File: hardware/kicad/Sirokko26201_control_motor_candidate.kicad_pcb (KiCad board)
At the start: 2 copper layers, 335 x 170 mm, 158 parts, among them J1 DEVKITC1_J1, J10 TC_K_EXHAUST_T+_T-, J102 MOTOR_24V_HIGH_SPEED; 125W_HE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, J11 TC_K_AIR_T+_T-, J12 ROOM_DS18B20_HARNESS, J13 24V_INPUT_PHOENIX_1756993_WIP, J22 START_STOP B3F-4055 + B32-138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, J23 ENCODER EC11E15244G1 + KNOB 4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, J24 RESET NKK BB25AB-FA, J26 TFT CABLE HARWIN M20-9960845 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, J27 GLOW_OUTPUT_PHOENIX_1756993, J28 CLUTCH_OUTPUT_PHOENIX_1756993, J3 DEVKITC1_J3, K1 DG85BM-5021-76-1024 + DZ85AB-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, K2 DG85BM-5021-76-1024 + DZ85AB-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, K3 DG85BM-5021-76-1024 + DZ85AB-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, Q1 IPB017N10N5LFATMA1 WIP, Q101 IRFB4110PBF (100V; RDS(on) @ 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, Q2 IPB017N10N5LFATMA1 WIP, Q20 BC847B,215, Q3 IPB017N10N5LFATMA1 WIP, Q4 IPB017N10N5LFATMA1 WIP, U1 TPS3431SDRBR, U10 MAX31856MUD+, U101 LM5013DDAR, U11 DRV8803PWPR, U13 LM74800QDRRRQ1 WIP_NOT_TRANSI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, U2 SN74HCS74D, U20 SN74LVC1G97DBVR, U301 TPS62162DSGR, U302 TPS3808G33DBVR, U303 74LVC125APW,118 Nexperia ONLY, U6 SN74HCS11D, U9 MAX31856MUD+, U9001 LTC7001IMSE#PBF; MSOP-10 EP, U9002 INA240A1ID, U9003 TLV9020DBVR, U9004 SN74LVC1G32DBVR, U9005 SN74LVC1G08DBVR, U9006 SN74LVC1G08DBVR, U9007 LM317HVT/NOPB TO-220; TJ 0…12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

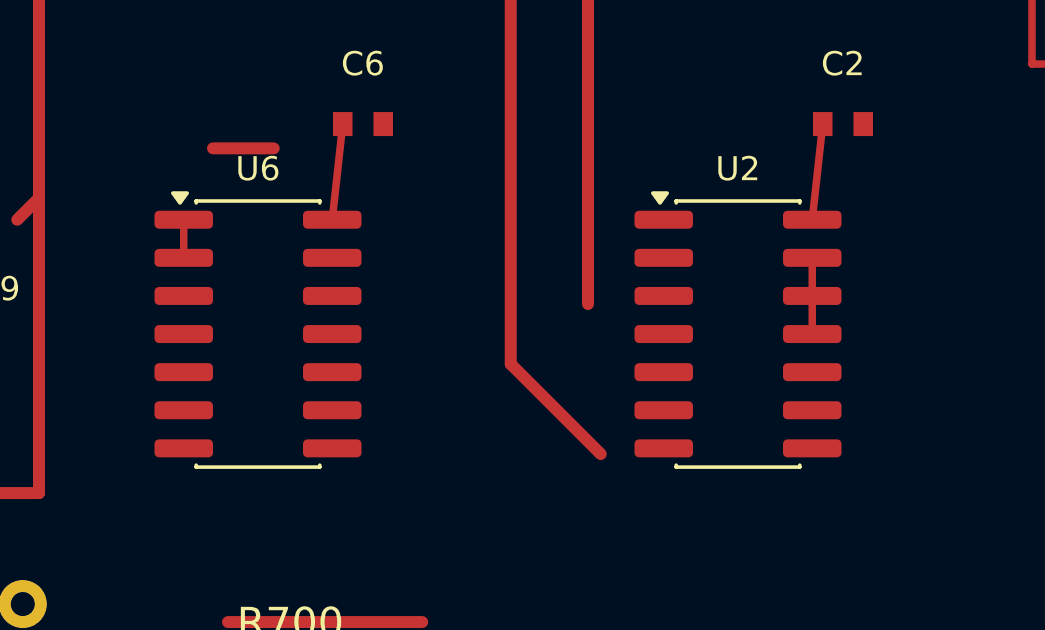
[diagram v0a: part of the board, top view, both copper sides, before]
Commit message: pcb: add after20 logic routing
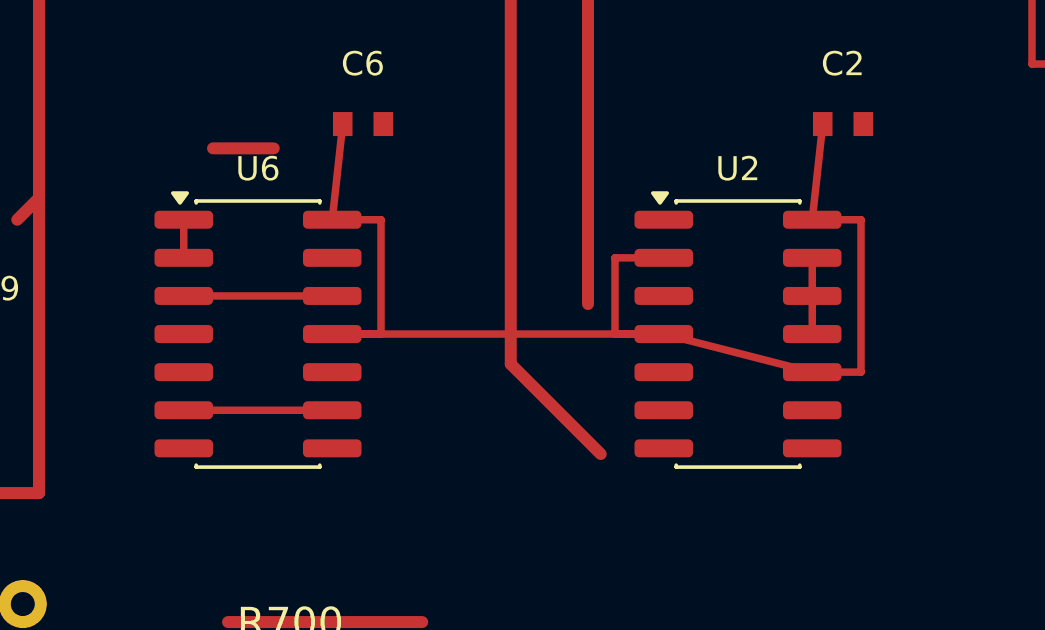
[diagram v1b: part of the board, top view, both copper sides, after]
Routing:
- net /+3V3: track 1245.0 -> 1282.4 mm
- net /MinimalSafety/RESET_POWER_READY: track 0.00 -> 4.95 mm
- net /MinimalSafety/HARD_CONDITIONS_OK: track 0.00 -> 4.95 mm
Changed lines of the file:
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@@
+		(net "/+3V3")
+	)
+	(segment
+		(start 49.475 61.19)
+		(end 51.1 61.19)
+		(width 0.25)
+		(layer "F.Cu")
+		(net "/+3V3")
+	)
+	(segment
+		(start 51.1 61.19)
+		(end 51.1 65)
+		(width 0.25)
+		(layer "F.Cu")
+		(net "/+3V3")
+	)
+	(segment
+		(start 51.1 65)
+		(end 49.475 65)
+		(width 0.25)
+		(layer "F.Cu")
+		(net "/+3V3")
+	)
+	(segment
+		(start 65.475 61.19)
+		(end 67.1 61.19)
+		(width 0.25)
+		(layer "F.Cu")
+		(net "/+3V3")
+	)
+	(segment
+		(start 67.1 61.19)
+		(end 67.1 66.27)
+		(width 0.25)
+		(layer "F.Cu")
+		(net "/+3V3")
+	)
+	(segment
+		(start 67.1 66.27)
+		(end 65.475 66.27)
+		(width 0.25)
+		(layer "F.Cu")
+		(net "/+3V3")
+	)
+	(segment
+		(start 60.525 62.46)
+		(end 58.9 62.46)
+		(width 0.25)
+		(layer "F.Cu")
+		(net "/+3V3")
+	)
+	(segment
+		(start 58.9 62.46)
+		(end 58.9 65)
+		(width 0.25)
+		(layer "F.Cu")
+		(net "/+3V3")
+	)
+	(segment
+		(start 58.9 65)
+		(end 60.525 65)
+		(width 0.25)
+		(layer "F.Cu")
+		(net "/+3V3")
+	)
+	(segment
+		(start 44.525 63.73)
+		(end 49.475 63.73)
+		(width 0.25)
+		(layer "F.Cu")
+		(net "/MinimalSafety/HARD_CONDITIONS_OK")
+	)
+	(segment
+		(start 44.525 67.54)
+		(end 49.475 67.54)
+		(width 0.25)
+		(layer "F.Cu")
+		(net "/MinimalSafety/RESET_POWER_READY")
+	)
+	(segment
+		(start 60.525 65)
+		(end 65.475 66.27)
+		(width 0.25)
+		(layer "F.Cu")
+		(net "/+3V3")
+	)
+	(segment
+		(start 49.475 65)
+		(end 55.425 65)
+		(width 0.25)
+		(layer "F.Cu")
+		(net "/+3V3")
+	)
+	(segment
+		(start 55.425 65)
+		(end 60.525 65)
+		(width 0.25)
+		(layer "F.Cu")
 		(net "/+3V3")
 	)

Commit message: pcb: add after30 routing
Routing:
- net /GND: track 2067.0 -> 2095.8 mm
- net /+3V3: track 1282.4 -> 1289.1 mm
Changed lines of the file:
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@@
 		(net "/+3V3")
+	)
+	(segment
+		(start 44.525 68.81)
+		(end 39.7 70.3)
+		(width 0.25)
+		(layer "F.Cu")
+		(net "/GND")
+	)
+	(segment
+		(start 60.525 68.81)
+		(end 53.16 77)
+		(width 0.25)
+		(layer "F.Cu")
+		(net "/GND")
+	)
+	(segment
+		(start 29.6 64.025)
+		(end 28.7 64.025)
+		(width 0.25)
+		(layer "F.Cu")
+		(net "/+3V3")
+	)
+	(segment
+		(start 28.7 64.025)
+		(end 28.7 65.325)
+		(width 0.25)
+		(layer "F.Cu")
+		(net "/+3V3")
+	)
+	(segment
+		(start 28.7 65.325)
+		(end 29.6 65.325)
+		(width 0.25)
+		(layer "F.Cu")
+		(net "/+3V3")
+	)
+	(segment
+		(start 29.6 64.025)
+		(end 27.675 61)
+		(width 0.25)
+		(layer "F.Cu")
+		(net "/+3V3")
+	)
+	(segment
+		(start 26.325 68.81)
+		(end 28.2 68.81)
+		(width 0.25)
+		(layer "F.Cu")
+		(net "/GND")
+	)
+	(segment
+		(start 26.325 61)
+		(end 24.8 61)
+		(width 0.25)
+		(layer "F.Cu")
+		(net "/GND")
+	)
+	(segment
+		(start 24.8 61)
+		(end 24.8 68.81)
+		(width 0.25)
+		(layer "F.Cu")
+		(net "/GND")
+	)
+	(segment
+		(start 24.8 68.81)
+		(end 26.325 68.81)
+		(width 0.25)
+		(layer "F.Cu")
+		(net "/GND")
 	)
 	(zone

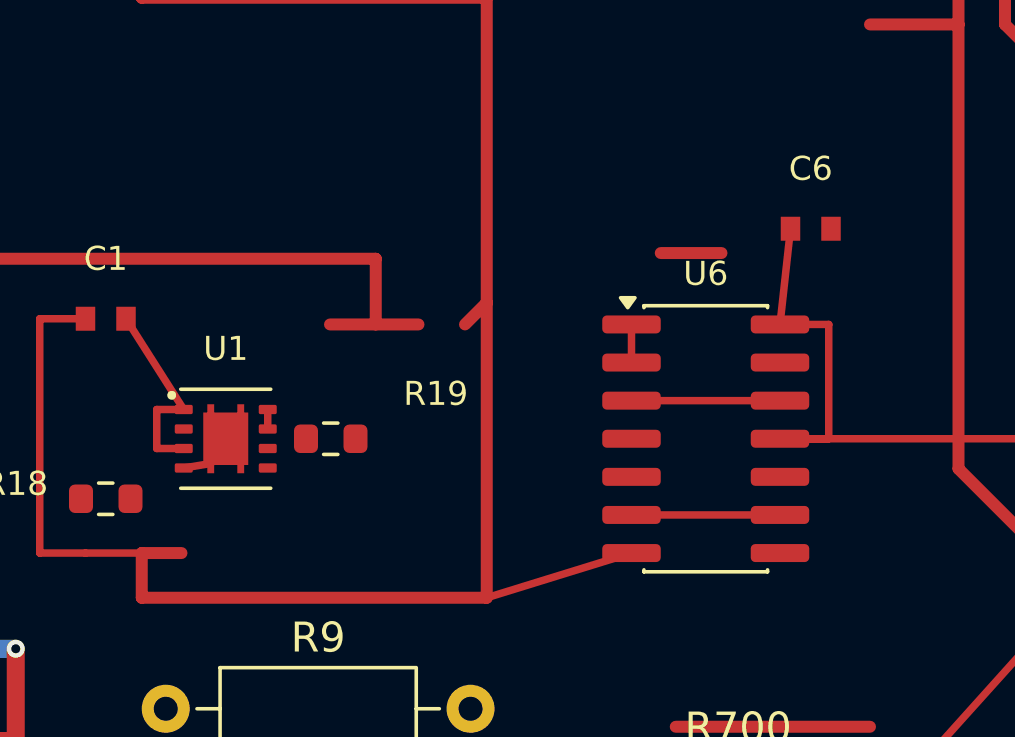
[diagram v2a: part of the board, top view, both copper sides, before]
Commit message: pcb: add after34 ground routing
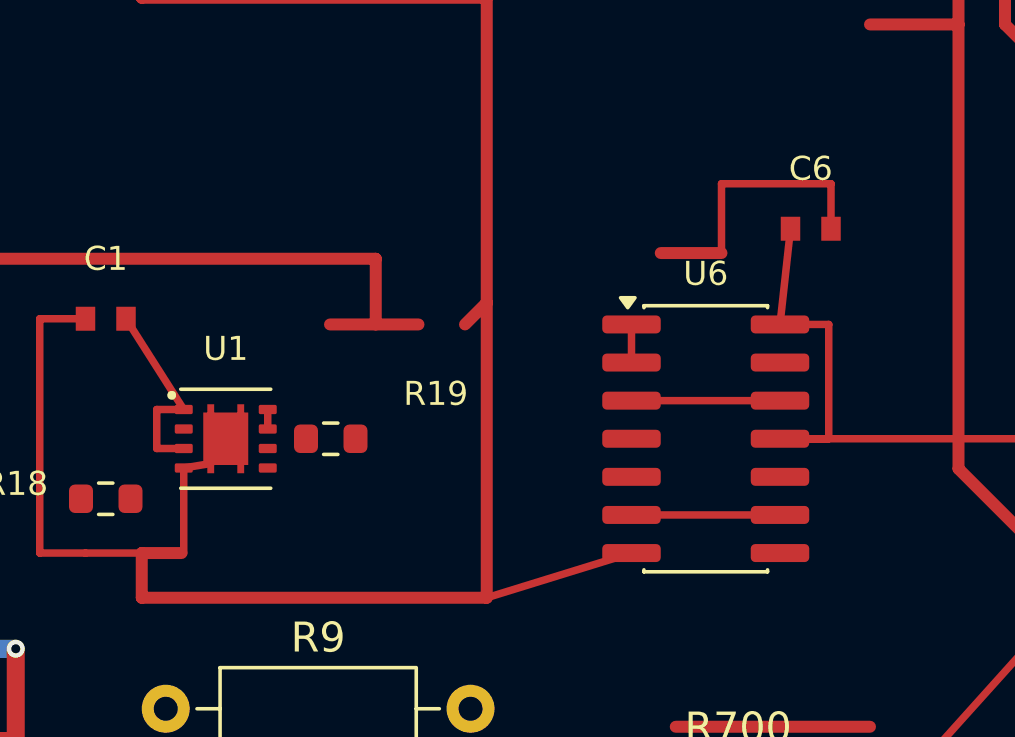
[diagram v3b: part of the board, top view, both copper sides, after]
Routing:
- net /GND: track 2095.8 -> 2106.1 mm
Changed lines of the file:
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@@
+		(net "/GND")
+	)
+	(segment
+		(start 29.6 65.975)
+		(end 29.6 68.81)
+		(width 0.25)
+		(layer "F.Cu")
+		(net "/GND")
+	)
+	(segment
+		(start 51.175 58)
+		(end 51.175 56.5)
+		(width 0.25)
+		(layer "F.Cu")
+		(net "/GND")
+	)
+	(segment
+		(start 51.175 56.5)
+		(end 47.525 56.5)
+		(width 0.25)
+		(layer "F.Cu")
+		(net "/GND")
+	)
+	(segment
+		(start 47.525 56.5)
+		(end 47.525 58.81)
+		(width 0.25)
+		(layer "F.Cu")
 		(net "/GND")
 	)

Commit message: pcb: add after42 3v3 routing
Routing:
- net /+3V3: track 1289.1 -> 1308.4 mm
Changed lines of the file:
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@@
 		(net "/GND")
+	)
+	(segment
+		(start 29.6 64.025)
+		(end 29.6 62.5)
+		(width 0.25)
+		(layer "F.Cu")
+		(net "/+3V3")
+	)
+	(segment
+		(start 29.6 62.5)
+		(end 34.475 62.5)
+		(width 0.25)
+		(layer "F.Cu")
+		(net "/+3V3")
+	)
+	(segment
+		(start 34.475 62.5)
+		(end 34.475 61.19)
+		(width 0.25)
+		(layer "F.Cu")
+		(net "/+3V3")
+	)
+	(segment
+		(start 26.175 67)
+		(end 26.175 64.025)
+		(width 0.25)
+		(layer "F.Cu")
+		(net "/+3V3")
+	)
+	(segment
+		(start 26.175 64.025)
+		(end 28.7 64.025)
+		(width 0.25)
+		(layer "F.Cu")
+		(net "/+3V3")
+	)
+	(segment
+		(start 33.675 65)
+		(end 33.675 65.975)
+		(width 0.25)
+		(layer "F.Cu")
+		(net "/+3V3")
+	)
+	(segment
+		(start 33.675 65.975)
+		(end 32.4 65.975)
+		(width 0.25)
+		(layer "F.Cu")
+		(net "/+3V3")
+	)
+	(segment
+		(start 33.675 65)
+		(end 34.475 61.19)
+		(width 0.25)
+		(layer "F.Cu")
+		(net "/+3V3")
 	)
 	(zone

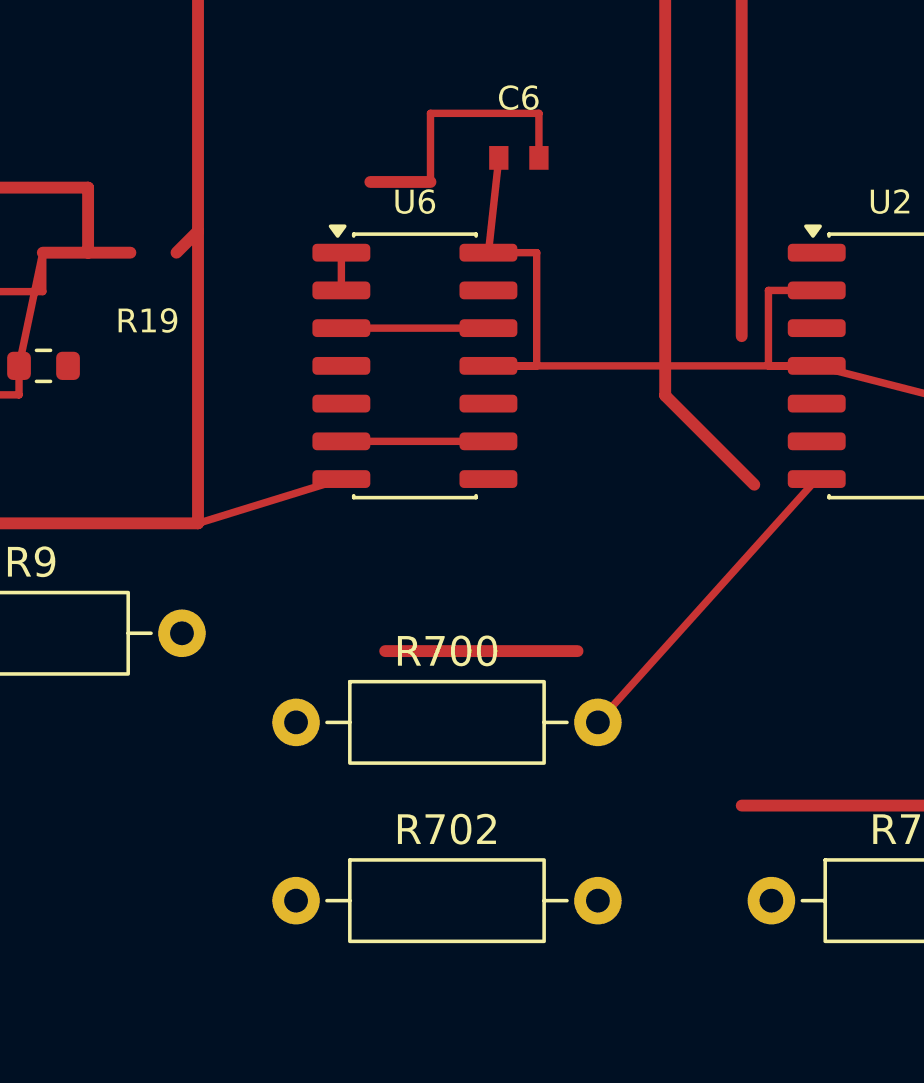
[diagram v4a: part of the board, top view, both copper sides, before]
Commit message: pcb: add after52 power and ground routing
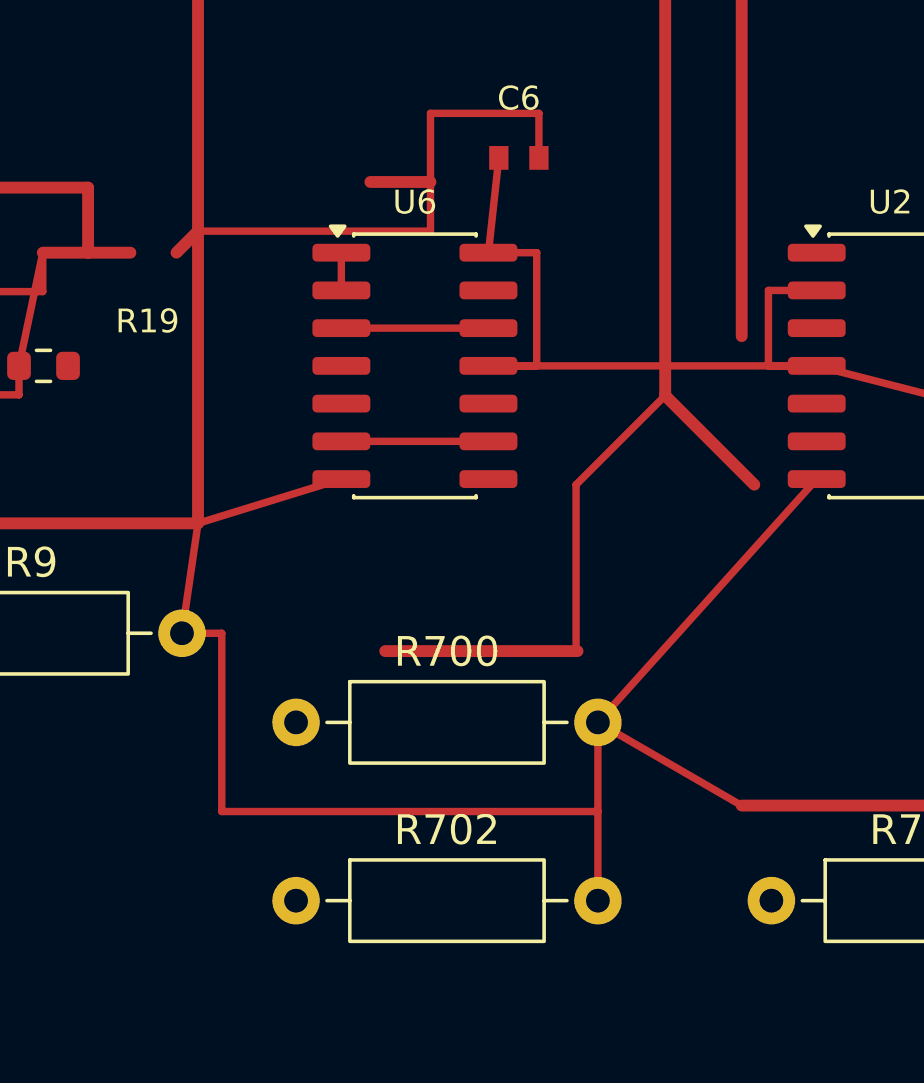
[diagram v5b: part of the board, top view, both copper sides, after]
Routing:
- net /GND: track 2106.1 -> 2150.9 mm
- net /+3V3: track 1308.4 -> 1318.3 mm
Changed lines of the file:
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@@
+		(net "/+3V3")
+	)
+	(segment
+		(start 47.525 58.81)
+		(end 47.525 60.465)
+		(width 0.25)
+		(layer "F.Cu")
+		(net "/GND")
+	)
+	(segment
+		(start 47.525 60.465)
+		(end 39.7 60.465)
+		(width 0.25)
+		(layer "F.Cu")
+		(net "/GND")
+	)
+	(segment
+		(start 39.7 70.3)
+		(end 39.16 74)
+		(width 0.25)
+		(layer "F.Cu")
+		(net "/GND")
+	)
+	(segment
+		(start 53.16 77)
+		(end 53.16 83)
+		(width 0.25)
+		(layer "F.Cu")
+		(net "/GND")
+	)
+	(segment
+		(start 53.16 77)
+		(end 58 79.8)
+		(width 0.25)
+		(layer "F.Cu")
+		(net "/GND")
+	)
+	(segment
+		(start 39.16 74)
+		(end 40.5 74)
+		(width 0.25)
+		(layer "F.Cu")
+		(net "/GND")
+	)
+	(segment
+		(start 40.5 74)
+		(end 40.5 80)
+		(width 0.25)
+		(layer "F.Cu")
+		(net "/GND")
+	)
+	(segment
+		(start 40.5 80)
+		(end 53.16 80)
+		(width 0.25)
+		(layer "F.Cu")
+		(net "/GND")
+	)
+	(segment
+		(start 55.425 66)
+		(end 52.425 69)
+		(width 0.25)
+		(layer "F.Cu")
+		(net "/+3V3")
+	)
+	(segment
+		(start 52.425 69)
+		(end 52.425 74.6)
+		(width 0.25)
+		(layer "F.Cu")
 		(net "/+3V3")
 	)

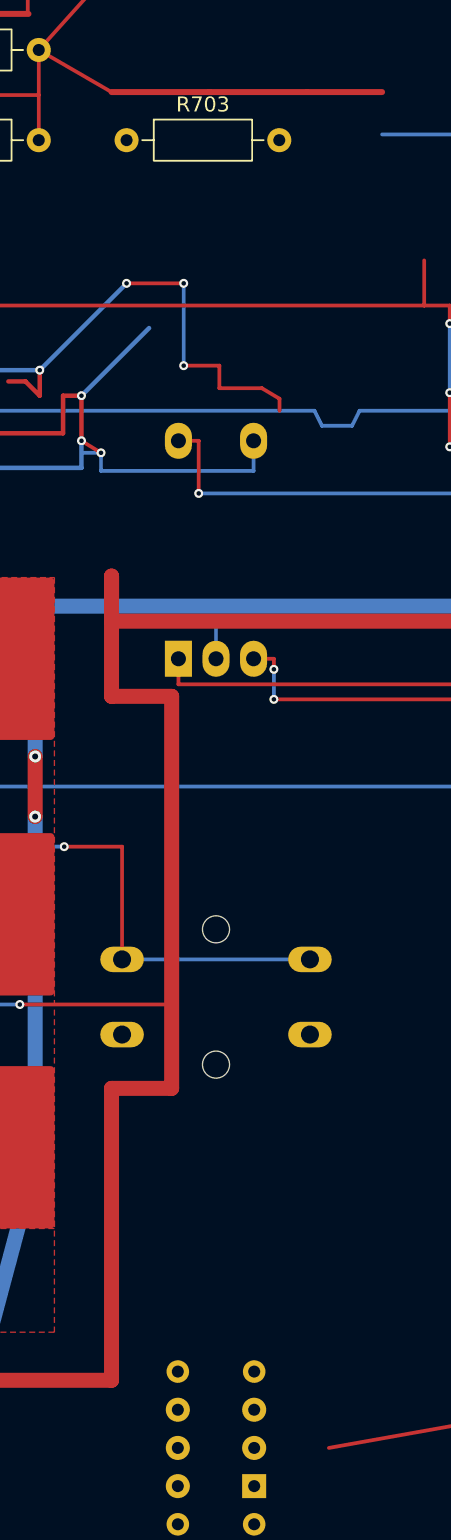
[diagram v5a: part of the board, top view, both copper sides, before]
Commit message: pcb: add after55 return routing
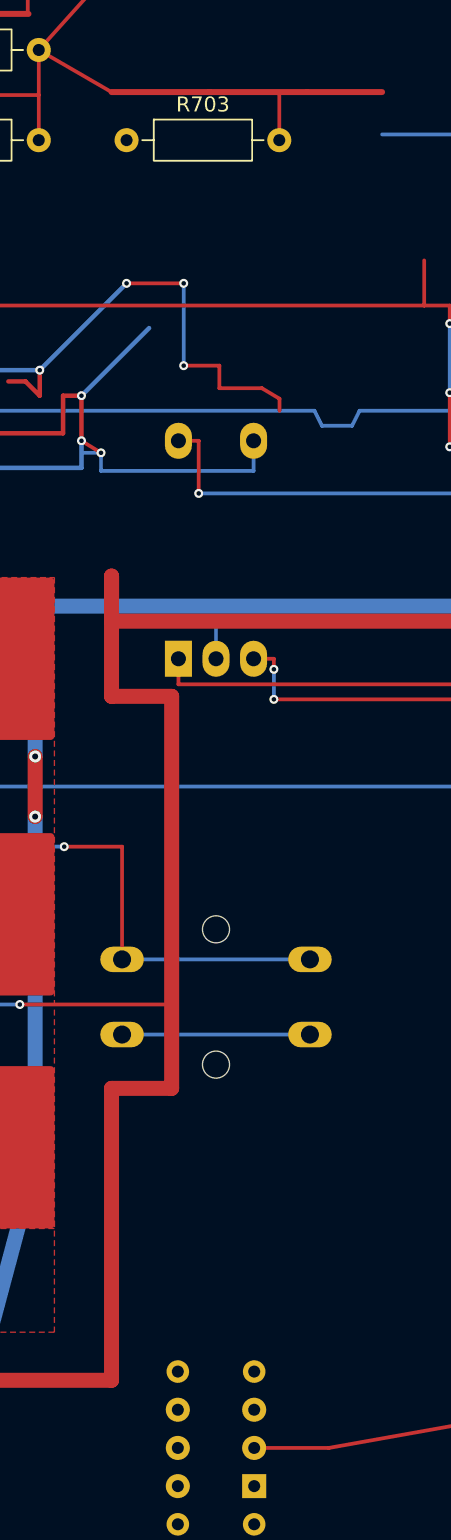
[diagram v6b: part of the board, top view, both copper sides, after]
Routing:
- net /START_REQUEST: track 0.00 -> 12.5 mm
- net /GND: track 2150.9 -> 2159.1 mm
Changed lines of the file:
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@@
 		(net "/+3V3")
+	)
+	(segment
+		(start 69.16 83)
+		(end 69.16 79.8)
+		(width 0.25)
+		(layer "F.Cu")
+		(net "/GND")
+	)
+	(segment
+		(start 67.49 170)
+		(end 72.46 170)
+		(width 0.25)
+		(layer "F.Cu")
+		(net "/GND")
+	)
+	(segment
+		(start 58.7 142.5)
+		(end 71.2 142.5)
+		(width 0.25)
+		(layer "B.Cu")
+		(net "/START_REQUEST")
 	)
 	(zone

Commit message: Add after63 native GND routing candidate
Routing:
- net /GND: track 2159.1 -> 2205.8 mm, vias 72 -> 74
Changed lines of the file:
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@@
 		(net "/START_REQUEST")
+	)
+	(segment
+		(start 65.475 65)
+		(end 64 65)
+		(width 0.25)
+		(layer "F.Cu")
+		(net "/GND")
+	)
+	(segment
+		(start 64.525 79.8)
+		(end 53.16 77)
+		(width 0.25)
+		(layer "B.Cu")
+		(net "/GND")
+	)
+	(segment
+		(start 69.16 79.8)
+		(end 64.525 79.8)
+		(width 0.25)
+		(layer "B.Cu")
+		(net "/GND")
+	)
+	(segment
+		(start 67.175 58)
+		(end 68.4 58)
+		(width 0.25)
+		(layer "F.Cu")
+		(net "/GND")
+	)
+	(segment
+		(start 64 65)
+		(end 53.16 77)
+		(width 0.25)
+		(layer "B.Cu")
+		(net "/GND")
+	)
+	(segment
+		(start 69.16 83)
+		(end 69.16 79.8)
+		(width 0.25)
+		(layer "B.Cu")
+		(net "/GND")
+	)
+	(segment
+		(start 68.4 58)
+		(end 64 65)
+		(width 0.25)
+		(layer "B.Cu")
+		(net "/GND")
+	)
+	(via
+		(at 64 65)
+		(size 0.6)
+		(drill 0.3)
+		(layers "F.Cu" "B.Cu")
+		(net "/GND")
+	)
+	(via
+		(at 68.4 58)
+		(size 0.6)
+		(drill 0.3)
+		(layers "F.Cu" "B.Cu")
+		(net "/GND")
 	)
 	(zone

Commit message: hardware: finish LM5013 feedback layout
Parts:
- moved R102 45.8 mm to (128.5, 55.8), turned to 180 degrees
- moved R101 37.1 mm to (133.0, 55.8), turned to 180 degrees
- moved C107 14.9 mm to (134.0, 58.0)
- moved C108 13.6 mm to (130.7, 58.3)
- moved R106 6.50 mm to (137.0, 56.5), turned to -90 degrees
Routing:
- net /LOGIC_POWER_24_TO_5V__DRAFT_NOT_FOR_ORDER/FB: track 54.3 -> 8.47 mm, vias 5 -> 0
- net +5V_DEVKIT: track 274.7 -> 298.0 mm
- net /GND: track 2205.8 -> 2207.9 mm, vias 74 -> 73
- net /LOGIC_POWER_24_TO_5V__DRAFT_NOT_FOR_ORDER/RAMP: track 9.83 -> 9.13 mm
